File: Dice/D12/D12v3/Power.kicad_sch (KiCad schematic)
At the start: 11 parts, among them U4 ME6215, U6 MT9700, U7 SN74LVC1G08, U8 TMR1366

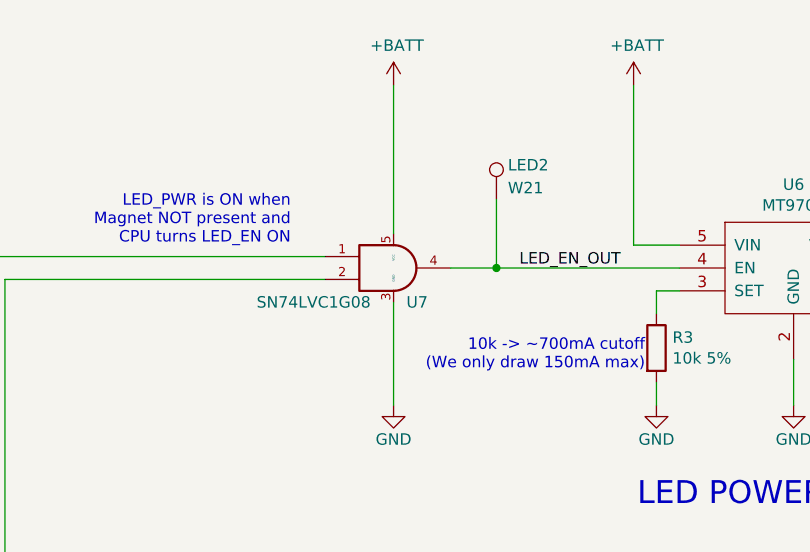
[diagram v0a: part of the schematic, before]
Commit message: New Version of All boards! Better Sticky tape shapes, tweaks to board outline, changed C19 footprint, revert coil pads to through holes. Also updated to Kicad 7.
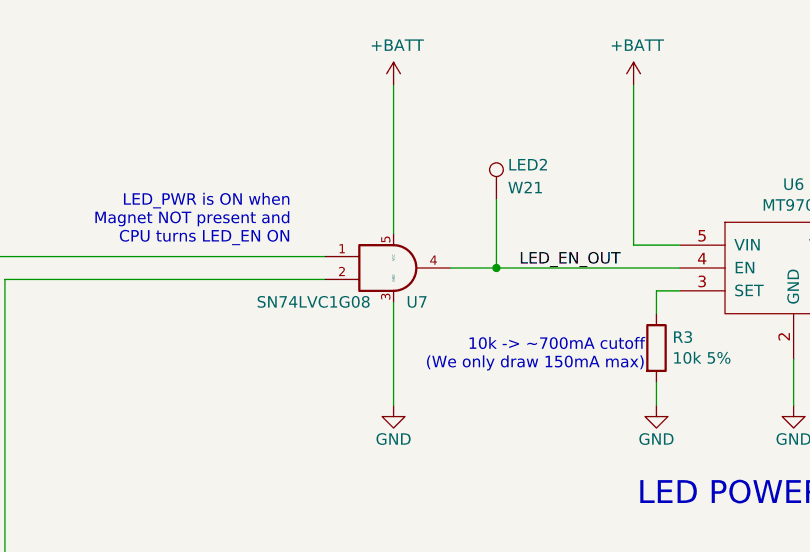
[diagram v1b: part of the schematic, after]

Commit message: Update C6/C19 Part number on all boards
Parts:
- C16, C9: Manufacturer Part Number GRM155R61A106ME44D -> GRM155R60J106ME05D
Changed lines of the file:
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@@
       (effects (font (size 1.27 1.27)) hide)
     )
-    (property "Manufacturer Part Number" "GRM155R61A106ME44D " (at 191.77 67.31 0)
+    (property "Manufacturer Part Number" "GRM155R60J106ME05D" (at 191.77 67.31 0)
       (effects (font (size 1.27 1.27)) hide)
     )
@@
       (effects (font (size 1.27 1.27)) hide)
     )
-    (property "Manufacturer Part Number" "GRM155R61A106ME44D " (at 118.11 134.62 0)
-      (effects (font (size 1.27 1.27)) hide)
-    )
+    (property "Manufacturer Part Number" "GRM155R60J106ME05D" (at 118.11 134.62 0)
+      (effects (font (size 1.27 1.27)) hide)
+    )
